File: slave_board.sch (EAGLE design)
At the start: 166 parts, among them IC1 NCP1117ST50T3G, IC2 NCP1117ST50T3G, IC3 ATMEGA2560-16AU, J11 1935161, J17 RJ45, J22 RJ45, J3 1935161, J6 1935161, K1 ORWH-SH-112D1F, Q1 PHB45NQ15T, Q2 PHB45NQ15T, Q3 BSS138L, Q5 BSS138L, Q7 PHB45NQ15T, Q8 IRFR9024TRPBF, U1 VNQ5E160KTR-E, U3 INA213AIDCKT, U4 VNH7070ASTR, U5 VNH7070ASTR, U6 VNQ5E160KTR-E, U7 INA213AIDCKT, Y1 ABLS-16.000MHZ-B4-T

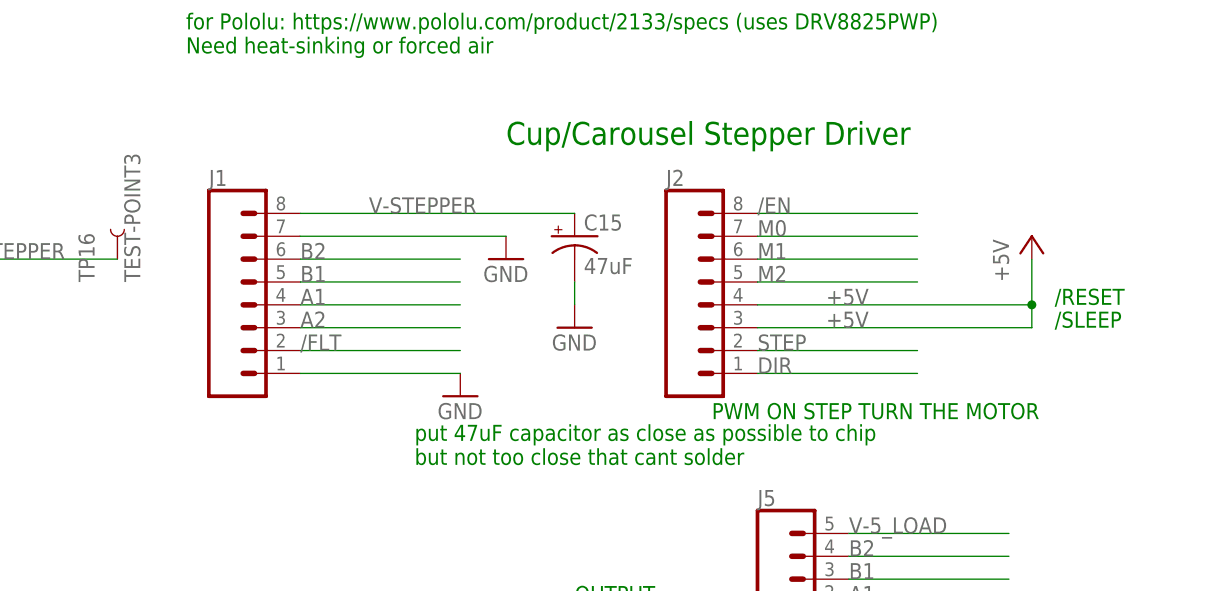
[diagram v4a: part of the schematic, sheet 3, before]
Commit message: turned motor driver into new part
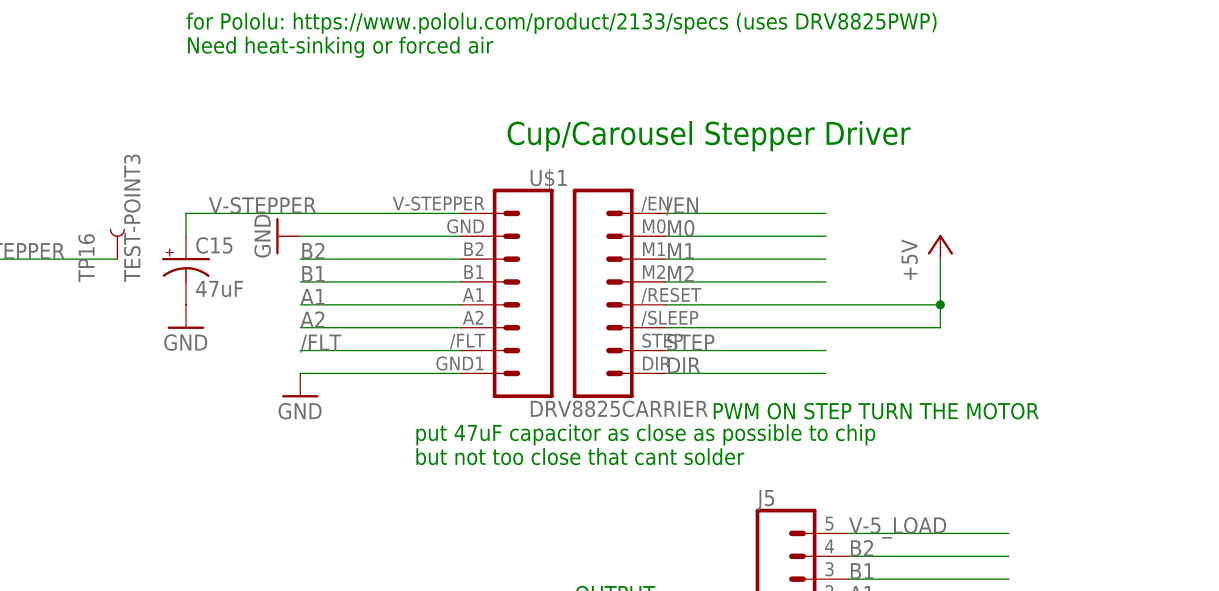
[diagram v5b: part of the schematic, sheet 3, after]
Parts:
- removed J1, J2: (no value), SparkFun-Connectors:CONN_08"
- added U$1: DRV8825CARRIER, smoothio:DRV8825CARRIER
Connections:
- new net N$8: U$1.2
- net +5V: now also U$1.11, U$1.12; no longer J2.3, J2.4
- net /EN: now also U$1.16; no longer J2.8
- net /FLT: now also U$1.7; no longer J1.2
- net A1: now also U$1.5; no longer J1.4
- net A2: now also U$1.6; no longer J1.3
- net B1: now also U$1.4; no longer J1.5
- net B2: now also U$1.3; no longer J1.6
- net DIR: now also U$1.9; no longer J2.1
- net GND: now also U$1.8; no longer J1.1, J1.7
- net M0: now also U$1.15; no longer J2.7
- net M1: now also U$1.14; no longer J2.6
- net M2: now also U$1.13; no longer J2.5
- net STEP: now also U$1.10; no longer J2.2
- net V-STEPPER: now also U$1.1; no longer J1.8
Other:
- note removed: "/RESET"
- note removed: "/SLEEP"
- moved on the sheet: C15

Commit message: Reviewed with Danyon
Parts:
- added C34: 0.1uF, SparkFun-Capacitors:0.1UF-0603-25V-(+80/-20%)
- added J1: (no value), SparkFun-Connectors:CONN_02
- added R23: 51K, SparkFun-Resistors:RESISTOR0603
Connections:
- net V-THERMISTOR renamed V-THERMISTOR0
- removed net STAT1_DIS: U1.STAT_DIS
- removed net STAT2_DIS: U6.STAT_DIS
- new net V-THERMISTOR1: C34.1, J1.2, R23.1
- net +5V: now also R23.2, U1.STAT_DIS, U6.STAT_DIS
- net GND: now also C34.2, J1.1
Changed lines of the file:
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@@
 <part name="GND29" library="supply1" library_urn="urn:adsk.eagle:library:371" deviceset="GND" device=""/>
 <part name="U$1" library="smoothio" deviceset="DRV8825CARRIER" device=""/>
+<part name="P+14" library="supply1" library_urn="urn:adsk.eagle:library:371" deviceset="+5V" device=""/>
+<part name="P+15" library="supply1" library_urn="urn:adsk.eagle:library:371" deviceset="+5V" device=""/>
+<part name="P+17" library="supply1" library_urn="urn:adsk.eagle:library:371" deviceset="+5V" device=""/>
+<part name="J1" library="SparkFun-Connectors" library_urn="urn:adsk.eagle:library:513" deviceset="CONN_02" device="" package3d_urn="urn:adsk.eagle:package:38039/1"/>
+<part name="P+18" library="supply1" library_urn="urn:adsk.eagle:library:371" deviceset="+5V" device=""/>
+<part name="GND52" library="supply1" library_urn="urn:adsk.eagle:library:371" deviceset="GND" device=""/>
+<part name="R23" library="SparkFun-Resistors" library_urn="urn:adsk.eagle:library:532" deviceset="RESISTOR" device="0603" package3d_urn="urn:adsk.eagle:package:39650/1" value=" 51K"/>
+<part name="C34" library="SparkFun-Capacitors" library_urn="urn:adsk.eagle:library:510" deviceset="0.1UF" device="-0603-25V-(+80/-20%)" package3d_urn="urn:adsk.eagle:package:37414/1" value="0.1uF"/>
 </parts>
 <sheets>
@@
 <attribute name="NAME" x="314.96" y="221.488" size="1.778" layer="95" font="vector"/>
 </instance>
+<instance part="P+14" gate="1" x="675.64" y="238.76" smashed="yes">
+<attribute name="VALUE" x="673.1" y="233.68" size="1.778" layer="96" rot="R90"/>
+</instance>
+<instance part="P+15" gate="1" x="43.18" y="190.5" smashed="yes">
+<attribute name="VALUE" x="40.64" y="185.42" size="1.778" layer="96" rot="R90"/>
+</instance>
+<instance part="P+17" gate="1" x="43.18" y="114.3" smashed="yes">
+<attribute name="VALUE" x="40.64" y="109.22" size="1.778" layer="96" rot="R90"/>
+</instance>
 </instances>
 <busses>
@@
 </segment>
 </net>
-<net name="STAT1_DIS" class="0">
-<segment>
-<pinref part="U1" gate="G$1" pin="STAT_DIS"/>
-<wire x1="63.5" y1="185.42" x2="55.88" y2="185.42" width="0.1524" layer="91"/>
-<label x="50.8" y="185.42" size="1.778" layer="95"/>
-</segment>
-</net>
 <net name="GND" class="2">
 <segment>
@@
 <wire x1="231.14" y1="30.48" x2="231.14" y2="25.4" width="0.1524" layer="91"/>
 </segment>
+<segment>
+<pinref part="U1" gate="G$1" pin="STAT_DIS"/>
+<pinref part="P+15" gate="1" pin="+5V"/>
+<wire x1="63.5" y1="185.42" x2="43.18" y2="185.42" width="0.1524" layer="91"/>
+<wire x1="43.18" y1="185.42" x2="43.18" y2="187.96" width="0.1524" layer="91"/>
+</segment>
+<segment>
+<pinref part="U6" gate="G$1" pin="STAT_DIS"/>
+<wire x1="63.5" y1="109.22" x2="48.26" y2="109.22" width="0.1524" layer="91"/>
+<pinref part="P+17" gate="1" pin="+5V"/>
+<wire x1="43.18" y1="111.76" x2="43.18" y2="109.22" width="0.1524" layer="91"/>
+<wire x1="43.18" y1="109.22" x2="48.26" y2="109.22" width="0.1524" layer="91"/>
+</segment>
 </net>
 <net name="+12V" class="0">
@@
 </segment>
 </net>
-<net name="STAT2_DIS" class="0">
-<segment>
-<pinref part="U6" gate="G$1" pin="STAT_DIS"/>
-<wire x1="63.5" y1="109.22" x2="50.8" y2="109.22" width="0.1524" layer="91"/>
-<label x="50.8" y="109.22" size="1.778" layer="95"/>
-</segment>
-</net>
 <net name="LIQUID1" class="0">
 <segment>
@@
 <attribute name="VALUE" x="179.324" y="147.701" size="1.778" layer="96" font="vector"/>
 </instance>
+<instance part="J1" gate="G$1" x="160.02" y="101.6" smashed="yes">
+<attribute name="VALUE" x="157.48" y="96.774" size="1.778" layer="96" font="vector"/>
+<attribute name="NAME" x="157.48" y="107.188" size="1.778" layer="95" font="vector"/>
+</instance>
+<instance part="P+18" gate="1" x="170.18" y="124.46" smashed="yes">
+<attribute name="VALUE" x="167.64" y="119.38" size="1.778" layer="96" rot="R90"/>
+</instance>
+<instance part="GND52" gate="1" x="170.18" y="86.36" smashed="yes">
+<attribute name="VALUE" x="167.64" y="83.82" size="1.778" layer="96"/>
+</instance>
+<instance part="R23" gate="G$1" x="170.18" y="114.3" smashed="yes" rot="R90">
+<attribute name="NAME" x="168.656" y="114.3" size="1.778" layer="95" font="vector" rot="R90" align="bottom-center"/>
+<attribute name="VALUE" x="171.704" y="114.3" size="1.778" layer="96" font="vector" rot="R90" align="top-center"/>
+</instance>
+<instance part="C34" gate="G$1" x="177.8" y="99.06" smashed="yes">
+<attribute name="NAME" x="179.324" y="101.981" size="1.778" layer="95" font="vector"/>
+<attribute name="VALUE" x="179.324" y="96.901" size="1.778" layer="96" font="vector"/>
+</instance>
 </instances>
 <busses>
@@
 <wire x1="73.66" y1="180.34" x2="68.58" y2="180.34" width="0.1524" layer="91"/>
 </segment>
+<segment>
+<wire x1="170.18" y1="119.38" x2="170.18" y2="121.92" width="0.1524" layer="91"/>
+<pinref part="P+18" gate="1" pin="+5V"/>
+<pinref part="R23" gate="G$1" pin="2"/>
+</segment>
 </net>
-<net name="V-THERMISTOR" class="2">
+<net name="V-THERMISTOR0" class="2">
 <segment>
 <label x="177.8" y="154.94" size="1.778" layer="95"/>
@@
 <junction x="55.88" y="187.96"/>
 </segment>
+<segment>
+<pinref part="GND52" gate="1" pin="GND"/>
+<pinref part="J1" gate="G$1" pin="1"/>
+<wire x1="170.18" y1="101.6" x2="167.64" y2="101.6" width="0.1524" layer="91"/>
+<wire x1="170.18" y1="101.6" x2="170.18" y2="93.98" width="0.1524" layer="91"/>
+<pinref part="C34" gate="G$1" pin="2"/>
+<wire x1="170.18" y1="93.98" x2="170.18" y2="88.9" width="0.1524" layer="91"/>
+<wire x1="177.8" y1="96.52" x2="177.8" y2="93.98" width="0.1524" layer="91"/>
+<wire x1="177.8" y1="93.98" x2="170.18" y2="93.98" width="0.1524" layer="91"/>
+<junction x="170.18" y="93.98"/>
+</segment>
 </net>
 <net name="CAROUSEL_POS" class="0">
@@
 </segment>
 </net>
+<net name="V-THERMISTOR1" class="0">
+<segment>
+<pinref part="J1" gate="G$1" pin="2"/>
+<pinref part="R23" gate="G$1" pin="1"/>
+<wire x1="167.64" y1="104.14" x2="170.18" y2="104.14" width="0.1524" layer="91"/>
+<wire x1="170.18" y1="109.22" x2="170.18" y2="104.14" width="0.1524" layer="91"/>
+<pinref part="C34" gate="G$1" pin="1"/>
+<wire x1="170.18" y1="104.14" x2="177.8" y2="104.14" width="0.1524" layer="91"/>
+<wire x1="177.8" y1="104.14" x2="185.42" y2="104.14" width="0.1524" layer="91"/>
+<label x="172.72" y="104.14" size="1.778" layer="95"/>
+</segment>
+</net>

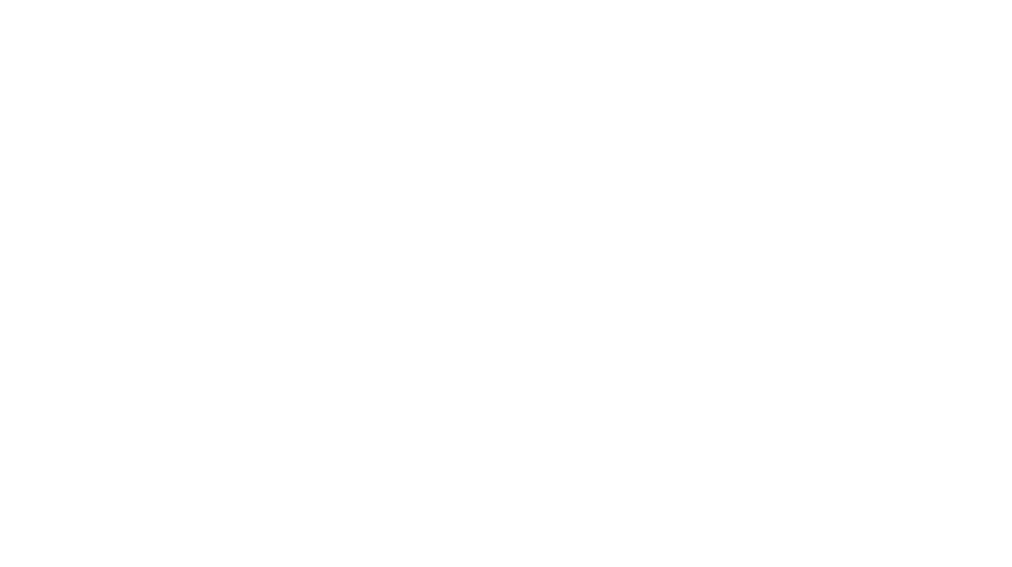
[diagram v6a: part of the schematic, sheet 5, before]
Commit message: Added encoders
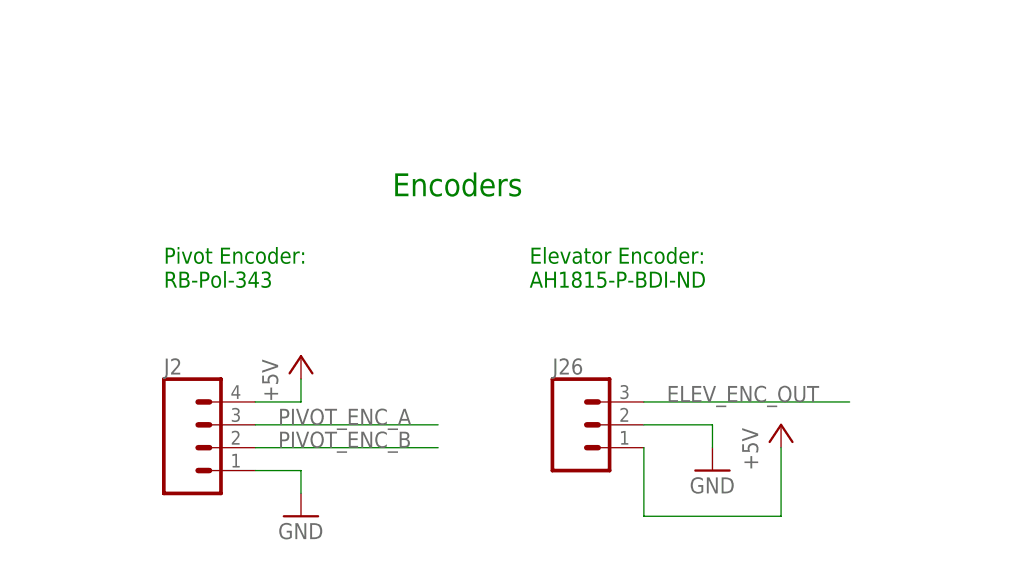
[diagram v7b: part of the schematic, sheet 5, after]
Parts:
- added J2: (no value), SparkFun-Connectors:CONN_041.27MM
- added J26: (no value), SparkFun-Connectors:CONN_03
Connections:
- new net ELEV_ENC_OUT: J26.3
- new net PIVOT_ENC_A: J2.3
- new net PIVOT_ENC_B: J2.2
- net +5V: now also J2.4, J26.1
- net GND: now also J2.1, J26.2
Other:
- note added: "Elevator Encoder: AH1815-P-BDI-ND"
- note added: "Encoders"
- note added: "Pivot Encoder: RB-Pol-343"
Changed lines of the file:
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@@
 <part name="R23" library="SparkFun-Resistors" library_urn="urn:adsk.eagle:library:532" deviceset="RESISTOR" device="0603" package3d_urn="urn:adsk.eagle:package:39650/1" value=" 51K"/>
 <part name="C34" library="SparkFun-Capacitors" library_urn="urn:adsk.eagle:library:510" deviceset="0.1UF" device="-0603-25V-(+80/-20%)" package3d_urn="urn:adsk.eagle:package:37414/1" value="0.1uF"/>
+<part name="J2" library="SparkFun-Connectors" deviceset="CONN_04" device="1.27MM"/>
+<part name="P+27" library="supply1" library_urn="urn:adsk.eagle:library:371" deviceset="+5V" device=""/>
+<part name="GND64" library="supply1" library_urn="urn:adsk.eagle:library:371" deviceset="GND" device=""/>
+<part name="J26" library="SparkFun-Connectors" deviceset="CONN_03" device=""/>
+<part name="GND66" library="supply1" library_urn="urn:adsk.eagle:library:371" deviceset="GND" device=""/>
+<part name="P+33" library="supply1" library_urn="urn:adsk.eagle:library:371" deviceset="+5V" device=""/>
 </parts>
 <sheets>
@@
 but less sensitivity at lower temps
 Need to tune</text>
+<text x="60.96" y="101.6" size="2.54" layer="91">Encoders</text>
+<text x="35.56" y="91.44" size="1.778" layer="91">Pivot Encoder:
+RB-Pol-343</text>
+<text x="76.2" y="91.44" size="1.778" layer="91">Elevator Encoder:
+AH1815-P-BDI-ND</text>
 </plain>
 <instances>
@@
 <attribute name="VALUE" x="179.324" y="96.901" size="1.778" layer="96" font="vector"/>
 </instance>
+<instance part="J2" gate="G$1" x="40.64" y="73.66" smashed="yes">
+<attribute name="VALUE" x="35.56" y="66.294" size="1.778" layer="96" font="vector"/>
+<attribute name="NAME" x="35.56" y="81.788" size="1.778" layer="95" font="vector"/>
+</instance>
+<instance part="P+27" gate="1" x="50.8" y="83.82" smashed="yes">
+<attribute name="VALUE" x="48.26" y="78.74" size="1.778" layer="96" rot="R90"/>
+</instance>
+<instance part="GND64" gate="1" x="50.8" y="66.04" smashed="yes">
+<attribute name="VALUE" x="48.26" y="63.5" size="1.778" layer="96"/>
+</instance>
+<instance part="J26" gate="J$1" x="81.28" y="76.2" smashed="yes">
+<attribute name="VALUE" x="75.946" y="63.5" size="1.778" layer="96" font="vector" rot="R90"/>
+<attribute name="NAME" x="78.74" y="81.788" size="1.778" layer="95" font="vector"/>
+</instance>
+<instance part="GND66" gate="1" x="96.52" y="71.12" smashed="yes">
+<attribute name="VALUE" x="93.98" y="68.58" size="1.778" layer="96"/>
+</instance>
+<instance part="P+33" gate="1" x="104.14" y="76.2" smashed="yes">
+<attribute name="VALUE" x="101.6" y="71.12" size="1.778" layer="96" rot="R90"/>
+</instance>
 </instances>
 <busses>
@@
 <pinref part="R23" gate="G$1" pin="2"/>
 </segment>
+<segment>
+<pinref part="J2" gate="G$1" pin="4"/>
+<wire x1="45.72" y1="78.74" x2="50.8" y2="78.74" width="0.1524" layer="91"/>
+<wire x1="50.8" y1="78.74" x2="50.8" y2="81.28" width="0.1524" layer="91"/>
+<pinref part="P+27" gate="1" pin="+5V"/>
+</segment>
+<segment>
+<pinref part="J26" gate="J$1" pin="1"/>
+<wire x1="88.9" y1="73.66" x2="88.9" y2="66.04" width="0.1524" layer="91"/>
+<wire x1="88.9" y1="66.04" x2="104.14" y2="66.04" width="0.1524" layer="91"/>
+<wire x1="104.14" y1="66.04" x2="104.14" y2="73.66" width="0.1524" layer="91"/>
+<pinref part="P+33" gate="1" pin="+5V"/>
+</segment>
 </net>
 <net name="V-THERMISTOR0" class="2">
@@
 <junction x="170.18" y="93.98"/>
 </segment>
+<segment>
+<pinref part="J2" gate="G$1" pin="1"/>
+<wire x1="45.72" y1="71.12" x2="50.8" y2="71.12" width="0.1524" layer="91"/>
+<wire x1="50.8" y1="71.12" x2="50.8" y2="68.58" width="0.1524" layer="91"/>
+<pinref part="GND64" gate="1" pin="GND"/>
+</segment>
+<segment>
+<pinref part="J26" gate="J$1" pin="2"/>
+<wire x1="88.9" y1="76.2" x2="96.52" y2="76.2" width="0.1524" layer="91"/>
+<wire x1="96.52" y1="76.2" x2="96.52" y2="73.66" width="0.1524" layer="91"/>
+<pinref part="GND66" gate="1" pin="GND"/>
+</segment>
 </net>
 <net name="CAROUSEL_POS" class="0">
@@
 </segment>
 </net>
+<net name="PIVOT_ENC_B" class="0">
+<segment>
+<pinref part="J2" gate="G$1" pin="2"/>
+<label x="48.26" y="73.66" size="1.778" layer="95"/>
+<wire x1="45.72" y1="73.66" x2="66.04" y2="73.66" width="0.1524" layer="91"/>
+</segment>
+</net>
+<net name="PIVOT_ENC_A" class="0">
+<segment>
+<pinref part="J2" gate="G$1" pin="3"/>
+<label x="48.26" y="76.2" size="1.778" layer="95"/>
+<wire x1="45.72" y1="76.2" x2="66.04" y2="76.2" width="0.1524" layer="91"/>
+</segment>
+</net>
+<net name="ELEV_ENC_OUT" class="0">
+<segment>
+<pinref part="J26" gate="J$1" pin="3"/>
+<wire x1="88.9" y1="78.74" x2="111.76" y2="78.74" width="0.1524" layer="91"/>
+<label x="91.44" y="78.74" size="1.778" layer="95"/>
+</segment>
+</net>
